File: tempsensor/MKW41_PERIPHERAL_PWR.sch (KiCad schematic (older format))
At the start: 34 parts, among them J3 Conn_ARM_JTAG_SWD_10, J4 USB_B_Micro, J5 Conn_01x02, SW3 ~RST, SW4 ~INT, U6 BQ24012

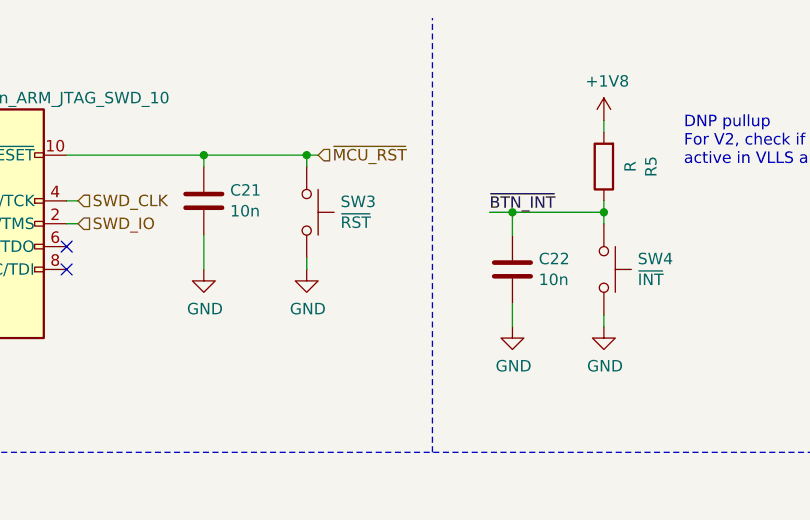
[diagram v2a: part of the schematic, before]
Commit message: Continued routing of tempsensor, basic functionality done.
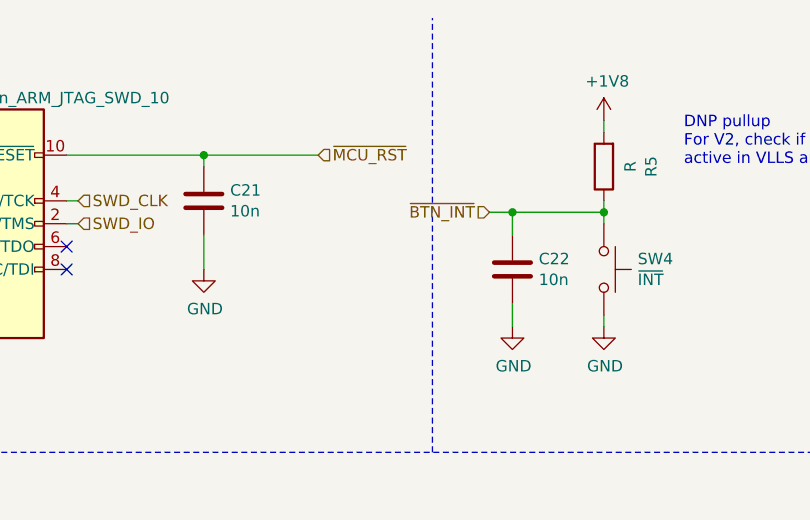
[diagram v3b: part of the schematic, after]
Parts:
- removed SW3: ~RST, Button_Switch_SMD:SW_SPST_Panasonic_EVQPL_3PL_5PL_PT_A08, symbol Switch:SW_Push
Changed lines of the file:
@@
-$EndComp
-$Comp
-L Switch:SW_Push SW?
-U 1 1 5FB6EE7F
-P 2550 1350
-AR Path="/5FB6EE7F" Ref="SW?"  Part="1"
-AR Path="/5FB5B55F/5FB6EE7F" Ref="SW3"  Part="1"
-F 0 "SW3" V 2504 1498 50  0000 L CNN
-F 1 "~RST" V 2595 1498 50  0000 L CNN
-F 2 "Button_Switch_SMD:SW_SPST_Panasonic_EVQPL_3PL_5PL_PT_A08" H 2550 1550 50  0001 C CNN
-F 3 "~" H 2550 1550 50  0001 C CNN
-	1    2550 1350
-	0    1    1    0
 $EndComp
 $Comp
@@
 Wire Wire Line
 	2100 1100 2100 1150
-Wire Wire Line
-	2100 1100 2550 1100
-Wire Wire Line
-	2550 1100 2550 1150
-$Comp
-L power:GND #PWR?
-U 1 1 5FB6EEB5
-P 2550 1600
-AR Path="/5FB6EEB5" Ref="#PWR?"  Part="1"
-AR Path="/5FB5B55F/5FB6EEB5" Ref="#PWR048"  Part="1"
-F 0 "#PWR048" H 2550 1350 50  0001 C CNN
-F 1 "GND" H 2555 1427 50  0000 C CNN
-F 2 "" H 2550 1600 50  0001 C CNN
-F 3 "" H 2550 1600 50  0001 C CNN
-	1    2550 1600
-	1    0    0    -1
-$EndComp
-Wire Wire Line
-	2550 1600 2550 1550
 NoConn ~ 1500 1500
 NoConn ~ 1500 1600
@@
 Wire Wire Line
 	3850 1850 3850 1800
-Wire Wire Line
-	3850 1350 3850 1400
-Text Label 3350 1350 0    50   ~ 0
-~BTN_INT
 Wire Wire Line
 	3350 1350 3450 1350
@@
 Wire Wire Line
 	3850 1300 3850 1350
-Connection ~ 3850 1350
 $Comp
 L power:+1V8 #PWR?
@@
 Text HLabel 2600 1100 2    50   Input ~ 0
 ~MCU_RST
-Wire Wire Line
-	2600 1100 2550 1100
-Connection ~ 2550 1100
 Text HLabel 1550 1300 2    50   Input ~ 0
 SWD_CLK
@@
 Wire Wire Line
 	650  7300 650  7500
+Wire Wire Line
+	2100 1100 2600 1100
+Wire Wire Line
+	3850 1400 3850 1350
+Connection ~ 3850 1350
+Text HLabel 3350 1350 0    50   Input ~ 0
+~BTN_INT
 $EndSCHEMATC

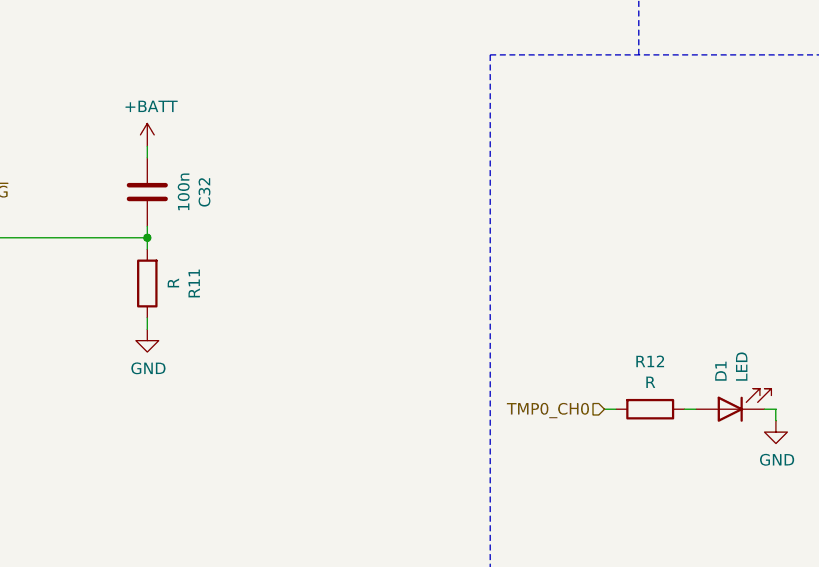
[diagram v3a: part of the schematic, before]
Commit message: Finished layouting tempsensor and thermostat. Parts are ordered from Mouser, PCB ordered from beta-layout.
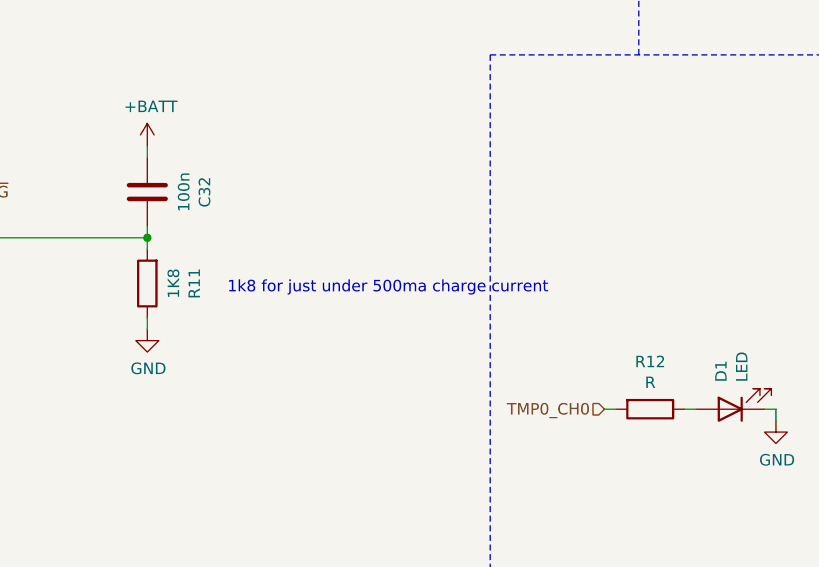
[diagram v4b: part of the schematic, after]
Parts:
- R11: value R -> 1K8
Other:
- note added: "1k8 for just under 500ma charge current"
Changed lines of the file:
@@
 AR Path="/5FB5B55F/5FBA3DF5" Ref="R11"  Part="1"
 F 0 "R11" V 5893 5250 50  0000 C CNN
-F 1 "R" V 5984 5250 50  0000 C CNN
+F 1 "1K8" V 5984 5250 50  0000 C CNN
 F 2 "Resistor_SMD:R_0402_1005Metric" V 6030 5250 50  0001 C CNN
 F 3 "~" H 6100 5250 50  0001 C CNN
@@
 Text HLabel 3350 1350 0    50   Input ~ 0
 ~BTN_INT
+Text Notes 6450 5300 0    50   ~ 0
+1k8 for just under 500ma charge current
 $EndSCHEMATC
